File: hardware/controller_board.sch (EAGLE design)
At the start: 105 parts, among them J1 FRSKY-GIMBAL-FRYSKY, J2 FRSKY-GIMBAL-FRYSKY, J3 USB-MICROB-EDAC-690-005-299-0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, J4 AVR_SPI_PRG_6NS, J8 FRSKY-GIMBAL-2X-SERVO, J9 FRSKY-GIMBAL-2X-SERVO, P6 10K, U1 ATMEGA128RFA1, U2 DPDT-X2, U3 FT232RLSSOP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

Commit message: Adjust encoder height.  Gimbal holes.  Servo connector placement.
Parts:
- removed B6: BATTERY, quadparts_prebuilt:BATTERY
- added B3: HEADER-0.1IN-2POS-SCREW, RemoteParts:HEADER-0.1IN-2POS-SCREW
- added J10: (no value), custom:MALE_HEADER_2POS-2X1-0.1IN
- added J11: USB-MICROA-AMPHENOL-10118192-0001LF, RemoteParts:USB-MICROA-AMPHENOL-10118192-0001LF
- added V3, V5: (no value), quadparts_prebuilt:LOCKED-VIA-0.2
- E1, E2, E3: value ROTARY-ENCODER-W/BUTTON-ADAFRUIT377-BOURNS-PEC12R -> ROTARY-ENCODER-W/BUTTON-BOURNS-PEC12R-30MM; device RemoteParts:ROTARY-ENCODER-W/BUTTON-ADAFRUIT377-BOURNS-PEC12R -> RemoteParts:ROTARY-ENCODER-W/BUTTON-BOURNS-PEC12R-30MM
- R13: value 9.09K -> 12K; device quadparts_prebuilt:RESISTOR_SMD-2012-0805-9.09K -> quadparts_prebuilt:RESISTOR_SMD-2012-0805-12K
- R14: value 33K -> 30K; device quadparts_prebuilt:RESISTOR_SMD-2012-0805-33K -> quadparts_prebuilt:RESISTOR_SMD-2012-0805-30K
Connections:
- removed net LCD-ENB: L1.E
- net BPOS: now also B3.1; no longer B6.P
- net GND: now also B3.2, J11.5-GND, V3.N, V5.N; no longer B6.N
- net LCD-E: now also L1.E
- net USB_D+: now also J11.3-D+
- net USB_D-: now also J11.2-D-
- net VBUS: now also J10.1, J10.2, J11.1-VCC
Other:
- note added: "This should map 4.2V to 3V."
- note removed: "This should map 4.2V to 3.3V."
- moved on the sheet: R13, R14

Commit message: added proper mounting holes
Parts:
- added U$1, U$3, U$6, U$7: MOUNTING-HOLE-M2.5-GROUNDED, RemoteParts:MOUNTING-HOLE-M2.5-GROUNDED
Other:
- note removed: "Power LED"
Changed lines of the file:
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@@
 <part name="V3" library="quadparts_prebuilt" deviceset="LOCKED-VIA" device="-0.2"/>
 <part name="V5" library="quadparts_prebuilt" deviceset="LOCKED-VIA" device="-0.2"/>
+<part name="U$1" library="RemoteParts" deviceset="MOUNTING-HOLE" device="-M2.5-GROUNDED"/>
+<part name="U$3" library="RemoteParts" deviceset="MOUNTING-HOLE" device="-M2.5-GROUNDED"/>
+<part name="U$6" library="RemoteParts" deviceset="MOUNTING-HOLE" device="-M2.5-GROUNDED"/>
+<part name="U$7" library="RemoteParts" deviceset="MOUNTING-HOLE" device="-M2.5-GROUNDED"/>
 </parts>
 <sheets>
 <sheet>
 <plain>
-<text x="5.08" y="104.14" size="1.778" layer="97">Power LED</text>
 <text x="204.47" y="143.51" size="1.778" layer="97">Ireg = 1000V/Rprog
 2.2KOhm -&gt; 450mA</text>
@@
 <instance part="V3" gate="G$1" x="144.78" y="182.88" rot="R90"/>
 <instance part="V5" gate="G$1" x="147.32" y="182.88" rot="R90"/>
+<instance part="U$1" gate="G$1" x="344.17" y="44.45"/>
+<instance part="U$3" gate="G$1" x="355.6" y="44.45"/>
+<instance part="U$6" gate="G$1" x="367.03" y="44.45"/>
+<instance part="U$7" gate="G$1" x="378.46" y="44.45"/>
 </instances>
 <busses>

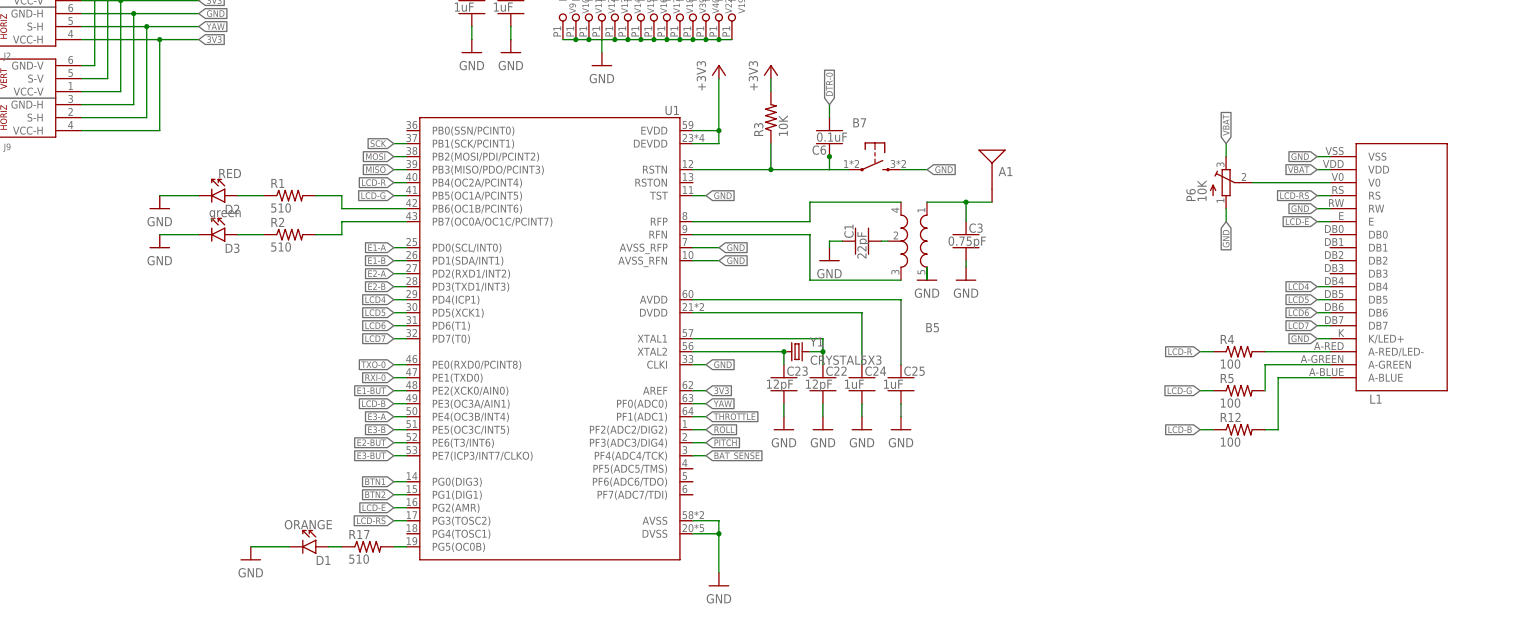
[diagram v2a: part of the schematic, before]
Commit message: Cleanly support monochrome and RGB LCDs.  Put all buttons and encoders on interrupts.  New pin assignments.  New uCtrl symbol
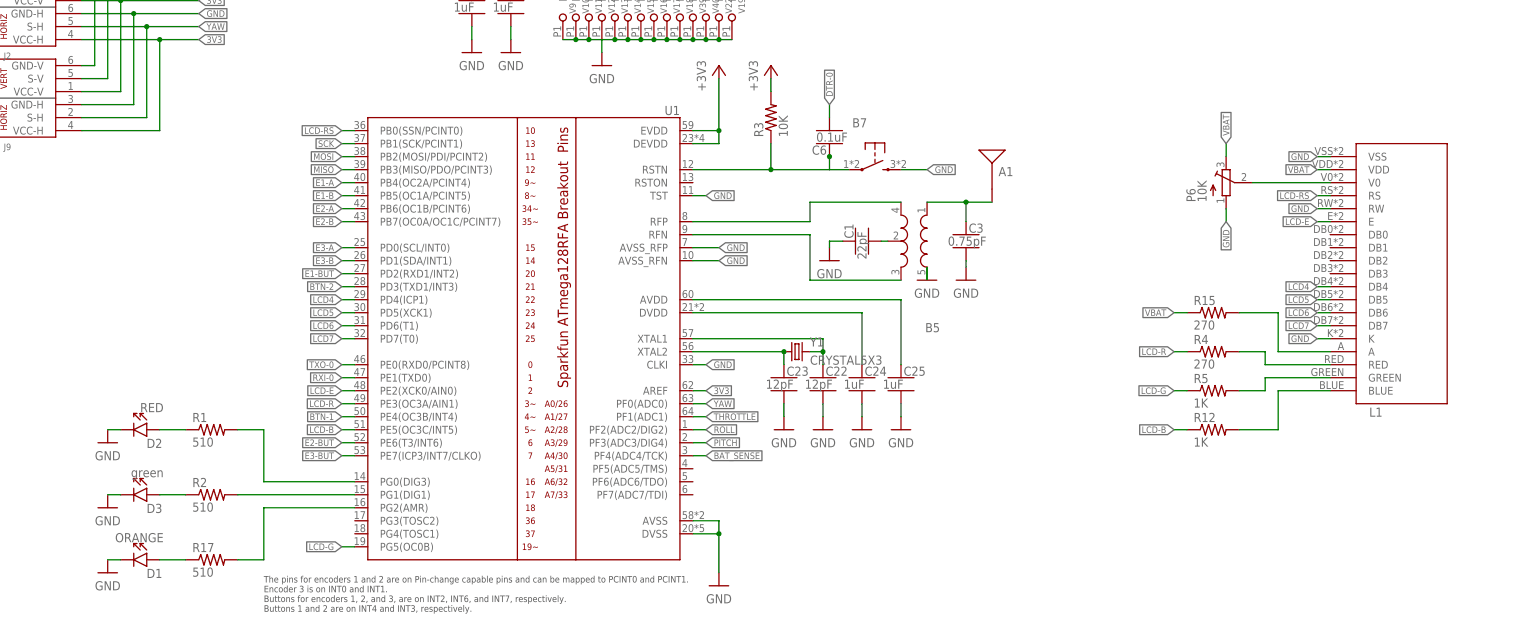
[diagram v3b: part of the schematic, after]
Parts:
- added R15: 270, quadparts_prebuilt:RESISTOR_SMD-2012-0805-270
- R12, R5: value 100 -> 1K; device quadparts_prebuilt:RESISTOR_SMD-2012-0805-100 -> quadparts_prebuilt:RESISTOR_SMD-2012-0805-1K
- R4: value 100 -> 270; device quadparts_prebuilt:RESISTOR_SMD-2012-0805-100 -> quadparts_prebuilt:RESISTOR_SMD-2012-0805-270
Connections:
- new net BTN-1: U1.PE4(OC3B/INT4)
- new net BTN-2: U1.PD3(TXD1/INT3)
- new net N$23: L1.A, R15.2
- net BTN1: no longer U1.PG0(DIG3)
- net BTN2: no longer U1.PG1(DIG1)
- net E1-A: now also U1.PB4(OC2A/PCINT4); no longer U1.PD0(SCL/INT0)
- net E1-B: now also U1.PB5(OC1A/PCINT5); no longer U1.PD1(SDA/INT1)
- net E1-BUT: now also U1.PD2(RXD1/INT2); no longer U1.PE2(XCK0/AIN0)
- net E2-A: now also U1.PB6(OC1B/PCINT6); no longer U1.PD2(RXD1/INT2)
- net E2-B: now also U1.PB7(OC0A/OC1C/PCINT7); no longer U1.PD3(TXD1/INT3)
- net E3-A: now also U1.PD0(SCL/INT0); no longer U1.PE4(OC3B/INT4)
- net E3-B: now also U1.PD1(SDA/INT1); no longer U1.PE5(OC3C/INT5)
- net GND: now also L1.K; no longer L1.K/LED+
- net LCD-B: now also U1.PE5(OC3C/INT5); no longer U1.PE3(OC3A/AIN1)
- net LCD-E: now also U1.PE2(XCK0/AIN0); no longer U1.PG2(AMR)
- net LCD-G: now also U1.PG5(OC0B); no longer U1.PB5(OC1A/PCINT5)
- net LCD-R: now also U1.PE3(OC3A/AIN1); no longer U1.PB4(OC2A/PCINT4)
- net LCD-RS: now also U1.PB0(SSN/PCINT0); no longer U1.PG3(TOSC2)
- net N$16: now also U1.PG2(AMR); no longer U1.PG5(OC0B)
- net N$17: now also L1.GREEN; no longer L1.A-GREEN
- net N$22: now also L1.BLUE; no longer L1.A-BLUE
- net N$4: now also U1.PG1(DIG1); no longer U1.PB7(OC0A/OC1C/PCINT7)
- net N$5: now also L1.RED; no longer L1.A-RED/LED-
- net N$8: now also U1.PG0(DIG3); no longer U1.PB6(OC1B/PCINT6)
- net VBAT: now also R15.1
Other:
- note added: "The pins for encoders 1 and 2 are on Pin-change capable pins and can be mapped to PCINT0 and PCINT1. Encoder 3 is on INT0 and INT1. Buttons for encoders 1, 2, and 3, are on INT2, INT6, and INT7, respectively. Buttons 1 and 2 are on INT4 and INT3, respectively."
- moved on the sheet: D1, D2, D3, R1, R12, R17, R2, R4, R5

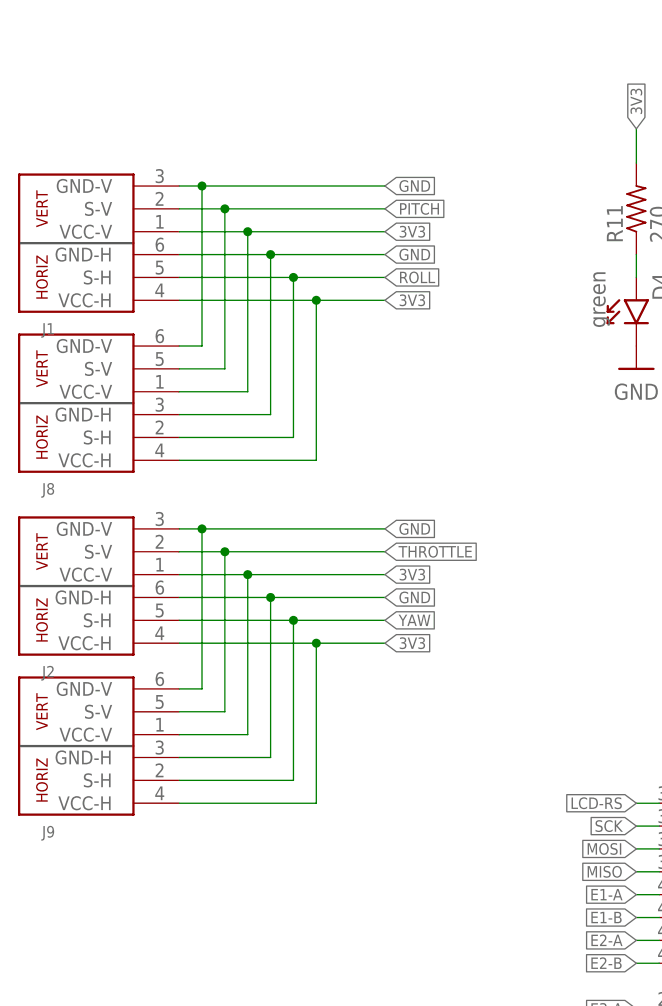
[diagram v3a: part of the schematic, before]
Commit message: new symbols for gimbals
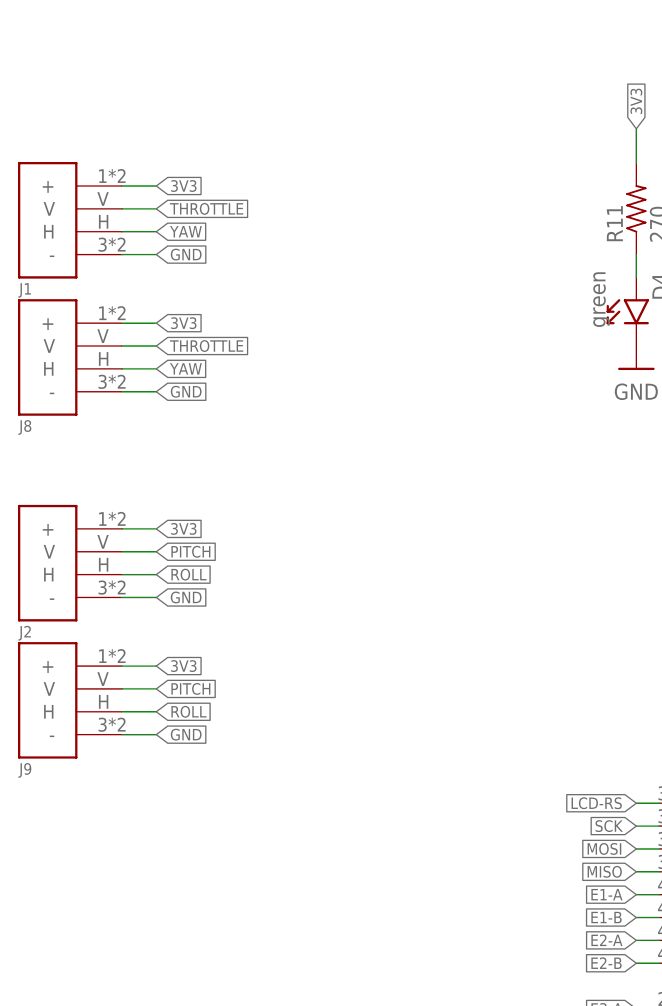
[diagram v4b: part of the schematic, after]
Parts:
- J1: CH1 PITCH -> (none); CH2 ROLL -> (none)
- J2: CH1 THR -> (none); CH2 YAW -> (none)
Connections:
- net 3V3: now also J1.+, J2.+, J8.+, J9.+; no longer J1.VCC-H, J1.VCC-V, J2.VCC-H, J2.VCC-V, J8.VCC-H, J8.VCC-V, J9.VCC-H, J9.VCC-V
- net GND: now also J1.-, J2.-, J8.-, J9.-; no longer J1.GND-H, J1.GND-V, J2.GND-H, J2.GND-V, J8.GND-H, J8.GND-V, J9.GND-H, J9.GND-V
- net PITCH: now also J2.V, J9.V; no longer J1.S-V, J8.S-V
- net ROLL: now also J2.H, J9.H; no longer J1.S-H, J8.S-H
- net THROTTLE: now also J1.V, J8.V; no longer J2.S-V, J9.S-V
- net YAW: now also J1.H, J8.H; no longer J2.S-H, J9.S-H

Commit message: support cheaper version.  Make the schematic pretty
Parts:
- added JP1, JP3, JP4, JP5: JUMPER-SMT_2_NO_SILK, RemoteParts:JUMPER-SMT_2_NO_SILK
- J10, J5, J6, J7: SPICEPREFIX (none) -> B
- J2: SPICEPREFIX (none) -> E
- L1: SPICEPREFIX (none) -> X
- P6: SPICEPREFIX (none) -> J
- R12, R15, R4, R5: SPICEPREFIX (none) -> R
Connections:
- net CTS-0: now also JP1.2
- net CTS-1: now also JP1.1
- net DTR-0: now also JP5.2
- net DTR-1: now also JP5.1
- net RXI-0: now also JP3.2
- net RXI-1: now also JP3.1
- net TXO-0: now also JP4.2
- net TXO-1: now also JP4.1
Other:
- note added: "Battery"
- note added: "FTDI Header"
- note added: "Frysky Gimbals"
- note added: "ISP"
- note added: "LCD"
- note added: "LiPo Charger"
- note added: "Power Breakouts"
- note added: "Rotary Encoders and Buttons"
- note added: "Servo Gimbals"
- note added: "Switchable FTDI"
- moved on the sheet: A1, B1, B2, B3, B5, B7, C1, C10, C11, C12, C13, C22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

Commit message: add separate 3.3v regulator
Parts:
- added C16, C17: 1uF, quadparts_prebuilt:CAPACITOR-NP_SMD-2012-0805_CERAMIC-1UF
- added U5: 3.3V, quadparts_prebuilt:TPS73633-DBVT3V3
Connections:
- net 3V3: now also C17.2, U5.OUT
- net GND: now also C16.2, C17.1, U5.GND
- net VBAT: now also C16.1, U5.EN, U5.IN
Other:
- note added: "150mA 3.3V Regulator *"
- note added: "Frysky Gimbals *"
- note added: "LCD *"
- note added: "LiPo Charger *"
- note added: "Power Breakouts *"
- note added: "Rotary Encoders and Buttons *"
- note added: "Servo Gimbals *"
- note added: "Switchable FTDI (& 70mA 3.3V regulator)*"
- note removed: "Frysky Gimbals"
- note removed: "LCD"
- note removed: "LiPo Charger"
- note removed: "Power Breakouts"
- note removed: "Rotary Encoders and Buttons"
- note removed: "Servo Gimbals"
- note removed: "Switchable FTDI"
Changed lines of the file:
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@@
 <part name="JP4" library="RemoteParts" deviceset="JUMPER-SMT_2_NO" device="_SILK"/>
 <part name="JP5" library="RemoteParts" deviceset="JUMPER-SMT_2_NO" device="_SILK"/>
+<part name="C16" library="quadparts_prebuilt" deviceset="CAPACITOR-NP_" device="SMD-2012-0805_CERAMIC-1UF" value="1uF"/>
+<part name="C17" library="quadparts_prebuilt" deviceset="CAPACITOR-NP_" device="SMD-2012-0805_CERAMIC-1UF" value="1uF"/>
+<part name="GND11" library="quadparts_prebuilt" deviceset="GND" device=""/>
+<part name="GND4" library="quadparts_prebuilt" deviceset="GND" device=""/>
+<part name="U5" library="quadparts_prebuilt" deviceset="TPS73633-DBVT" device="3V3" value="3.3V"/>
 </parts>
 <sheets>
@@
 <wire x1="77.47" y1="64.77" x2="311.15" y2="64.77" width="0.1524" layer="97" style="longdash"/>
 <wire x1="311.15" y1="64.77" x2="311.15" y2="130.81" width="0.1524" layer="97" style="longdash"/>
-<text x="85.09" y="6.35" size="3.81" layer="97">LiPo Charger</text>
-<text x="196.85" y="66.04" size="3.81" layer="97">Switchable FTDI</text>
+<text x="85.09" y="6.35" size="3.81" layer="97">LiPo Charger *</text>
+<text x="154.94" y="66.04" size="3.81" layer="97">Switchable FTDI (&amp; 70mA 3.3V regulator)*</text>
 <wire x1="63.5" y1="275.59" x2="63.5" y2="226.06" width="0.1524" layer="97" style="longdash"/>
 <wire x1="63.5" y1="226.06" x2="3.81" y2="226.06" width="0.1524" layer="97" style="longdash"/>
@@
 <wire x1="63.5" y1="181.61" x2="63.5" y2="135.89" width="0.1524" layer="97" style="longdash"/>
 <wire x1="63.5" y1="135.89" x2="3.81" y2="135.89" width="0.1524" layer="97" style="longdash"/>
-<text x="6.35" y="227.33" size="3.81" layer="97">Power Breakouts</text>
-<text x="7.62" y="184.15" size="3.81" layer="97">Frysky Gimbals</text>
-<text x="7.62" y="138.43" size="3.81" layer="97">Servo Gimbals</text>
+<text x="6.35" y="227.33" size="3.81" layer="97">Power Breakouts *</text>
+<text x="7.62" y="184.15" size="3.81" layer="97">Frysky Gimbals *</text>
+<text x="7.62" y="138.43" size="3.81" layer="97">Servo Gimbals *</text>
 <wire x1="328.93" y1="275.59" x2="328.93" y2="196.85" width="0.1524" layer="97" style="longdash"/>
 <wire x1="328.93" y1="196.85" x2="427.99" y2="196.85" width="0.1524" layer="97" style="longdash"/>
-<text x="344.17" y="199.39" size="3.81" layer="97">Rotary Encoders and Buttons</text>
+<text x="344.17" y="199.39" size="3.81" layer="97">Rotary Encoders and Buttons *</text>
 <wire x1="208.28" y1="59.69" x2="270.51" y2="59.69" width="0.1524" layer="97" style="longdash"/>
 <wire x1="270.51" y1="59.69" x2="270.51" y2="3.81" width="0.1524" layer="97" style="longdash"/>
@@
 <wire x1="328.93" y1="196.85" x2="327.66" y2="114.3" width="0.1524" layer="97" style="longdash"/>
 <wire x1="327.66" y1="114.3" x2="426.72" y2="114.3" width="0.1524" layer="97" style="longdash"/>
-<text x="370.84" y="116.84" size="3.81" layer="97">LCD</text>
+<text x="370.84" y="116.84" size="3.81" layer="97">LCD *</text>
 <wire x1="327.66" y1="114.3" x2="327.66" y2="78.74" width="0.1524" layer="97" style="longdash"/>
 <wire x1="327.66" y1="78.74" x2="427.99" y2="78.74" width="0.1524" layer="97" style="longdash"/>
@@
 <text x="373.38" y="82.55" size="3.81" layer="97">ISP</text>
 <text x="361.95" y="39.37" size="3.81" layer="97">FTDI Header</text>
+<wire x1="63.5" y1="135.89" x2="63.5" y2="99.06" width="0.1524" layer="97" style="longdash"/>
+<wire x1="63.5" y1="99.06" x2="3.81" y2="99.06" width="0.1524" layer="97" style="longdash"/>
+<text x="5.08" y="100.33" size="3.81" layer="97">150mA 3.3V Regulator *</text>
 </plain>
 <instances>
@@
 <instance part="JP4" gate="G$1" x="365.76" y="60.96"/>
 <instance part="JP5" gate="G$1" x="365.76" y="55.88"/>
+<instance part="C16" gate="G$1" x="10.16" y="123.19"/>
+<instance part="C17" gate="G$1" x="53.34" y="120.65" rot="R180"/>
+<instance part="GND11" gate="1" x="53.34" y="113.03"/>
+<instance part="GND4" gate="1" x="22.86" y="118.11"/>
+<instance part="U5" gate="G$1" x="27.94" y="113.03"/>
 </instances>
 <busses>
@@
 <label x="30.48" y="163.83" size="1.27" layer="95" xref="yes"/>
 </segment>
+<segment>
+<pinref part="C17" gate="G$1" pin="1"/>
+<pinref part="GND11" gate="1" pin="GND"/>
+<wire x1="53.34" y1="118.11" x2="53.34" y2="115.57" width="0.1524" layer="91"/>
+</segment>
+<segment>
+<pinref part="GND4" gate="1" pin="GND"/>
+<pinref part="U5" gate="G$1" pin="GND"/>
+<wire x1="25.4" y1="120.65" x2="22.86" y2="120.65" width="0.1524" layer="91"/>
+</segment>
+<segment>
+<pinref part="C16" gate="G$1" pin="2"/>
+<wire x1="10.16" y1="113.03" x2="10.16" y2="118.11" width="0.1524" layer="91"/>
+<label x="10.16" y="113.03" size="1.27" layer="95" xref="yes"/>
+</segment>
 </net>
 <net name="BTN1" class="0">
@@
 <wire x1="26.67" y1="171.45" x2="30.48" y2="171.45" width="0.1524" layer="91"/>
 <label x="30.48" y="171.45" size="1.27" layer="95" xref="yes"/>
+</segment>
+<segment>
+<pinref part="C17" gate="G$1" pin="2"/>
+<pinref part="U5" gate="G$1" pin="OUT"/>
+<wire x1="48.26" y1="125.73" x2="53.34" y2="125.73" width="0.1524" layer="91"/>
+<label x="53.34" y="125.73" size="1.27" layer="95" xref="yes"/>
 </segment>
 </net>
@@
 <label x="351.79" y="152.4" size="1.27" layer="95" rot="R180" xref="yes"/>
 </segment>
-</net>
+<segment>
+<pinref part="C16" gate="G$1" pin="1"/>
+<junction x="10.16" y="125.73"/>
+<pinref part="U5" gate="G$1" pin="EN"/>
+<wire x1="17.78" y1="125.73" x2="10.16" y2="125.73" width="0.1524" layer="91"/>
+<wire x1="17.78" y1="115.57" x2="25.4" y2="115.57" width="0.1524" layer="91"/>
+<wire x1="17.78" y1="125.73" x2="17.78" y2="115.57" width="0.1524" layer="91"/>
+<pinref part="U5" gate="G$1" pin="IN"/>
+<wire x1="25.4" y1="125.73" x2="17.78" y2="125.73" width="0.1524" layer="91"/>
+<junction x="17.78" y="125.73"/>
+</segment>
+</net>
